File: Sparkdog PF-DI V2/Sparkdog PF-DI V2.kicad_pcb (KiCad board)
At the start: 2 copper layers, 124.5 x 98.9 mm, 3 parts

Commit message: Commit schematic changes, new parts library footprints and step files, PCB design file.
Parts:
- removed IC**: SOP65P1420X360-37N, Samacsys:SOP65P1420X360-37N
- removed REF**: TEENSY_3_5, Sparkdog PF-DI V2:TEENSY_3_5
- removed REF**: ARDUINO_DUE, Sparkdog PF-DI V2:ARDUINO_DUE
- added C200: 0603 1nF, Samacsys:RESC1608X55N, F.Cu at (150.1, 104.0)
- added C201: 0603 1nF, Samacsys:RESC1608X55N, F.Cu at (131.1, 98.0)
- added C202: 0603 1nF, Samacsys:RESC1608X55N, F.Cu at (149.5, 89.7)
- added C203: 0603 1nF, Samacsys:RESC1608X55N, F.Cu at (150.9, 100.5)
- added C400: 0603 100nF, Samacsys:RESC1608X55N, F.Cu at (54.2, 143.8)
- added C401: 0603 100nF, Samacsys:RESC1608X55N, F.Cu at (54.2, 137.8)
- added C402: 0603 1nF, Samacsys:RESC1608X55N, F.Cu at (54.2, 141.0)
- added C403: 0603 1nF, Samacsys:RESC1608X55N, F.Cu at (51.3, 133.6)
- added C404: 0603 1nF, Samacsys:RESC1608X55N, F.Cu at (51.3, 143.8)
- added C405: 0603 1nF, Samacsys:RESC1608X55N, F.Cu at (51.3, 137.8)
- added C500: 0603 10nF, Samacsys:RESC1608X55N, F.Cu at (79.2, 160.1)
- added C501: 0603 10nF, Samacsys:RESC1608X55N, F.Cu at (107.4, 167.9)
- added C502: 0603 10nF, Samacsys:RESC1608X55N, F.Cu at (82.4, 160.1)
- added C503: 0603 100nF, Samacsys:RESC1608X55N, F.Cu at (78.6, 155.1)
- added C504: 0603 100nF, Samacsys:RESC1608X55N, F.Cu at (102.4, 158.9)
- added C505: 0805 10uF, Samacsys:RESC2012X60N, F.Cu at (59.6, 112.6)
- added C506: 0805 10uF, Samacsys:RESC2012X60N, F.Cu at (59.6, 115.8)
- added C600: 0603 10pF, Samacsys:RESC1608X55N, F.Cu at (126.9, 144.3)
- added C601: 0603 10pF, Samacsys:RESC1608X55N, F.Cu at (126.0, 147.6)
- added C700: 0603 100nF, Samacsys:RESC1608X55N, F.Cu at (60.8, 152.8)
- added C701: 0603 10pF, Samacsys:RESC1608X55N, F.Cu at (150.2, 127.0)
- added C702: 0603 10pF, Samacsys:RESC1608X55N, F.Cu at (137.4, 131.6)
- added CD200: 0603 100nF, Samacsys:RESC1608X55N, F.Cu at (146.4, 89.7)
- added CD400: 0603 100nF, Samacsys:RESC1608X55N, F.Cu at (47.0, 139.3)
- added CD401: 0603 100nF, Samacsys:RESC1608X55N, F.Cu at (47.5, 133.0)
- added CD500: CAP4mm 4.7uF, Samacsys:CAPAE1700X1700N, F.Cu at (115.7, 160.8)
- added CD501: 0603 100nF, Samacsys:RESC1608X55N, F.Cu at (87.5, 154.4)
- added CD502: 0603 100nF, Samacsys:RESC1608X55N, F.Cu at (66.5, 112.6)
- added CD600: 0603 100nF, Samacsys:RESC1608X55N, F.Cu at (125.5, 150.4)
- added CD601: 0603 100nF, Samacsys:RESC1608X55N, F.Cu at (127.0, 132.6)
- added CD602: 0603 100nF, Samacsys:RESC1608X55N, F.Cu at (124.6, 148.1)
- added CD603: 0603 100nF, Samacsys:RESC1608X55N, F.Cu at (108.5, 145.3)
- added CD604: 0603 100nF, Samacsys:RESC1608X55N, F.Cu at (131.6, 134.9)
- added CD605: 0603 100nF, Samacsys:RESC1608X55N, F.Cu at (108.0, 136.4)
- added CD606: 0603 100nF, Samacsys:RESC1608X55N, F.Cu at (128.9, 137.4)
- added CD700: 0603 100nF, Samacsys:RESC1608X55N, F.Cu at (141.5, 141.6)
- added CD701: 0603 100nF, Samacsys:RESC1608X55N, F.Cu at (136.0, 147.1)
- added CD702: CAP4mm 4.7uF, Samacsys:CAPAE430X550N, F.Cu at (141.6, 145.2)
- added CD703: 0603 100nF, Samacsys:RESC1608X55N, F.Cu at (135.4, 134.0)
- added CD704: CAP4mm 4.7uF, Samacsys:CAPAE430X550N, F.Cu at (137.8, 150.7)
- added CD705: 0603 100nF, Samacsys:RESC1608X55N, F.Cu at (129.8, 133.3)
- added CD706: 0603 100nF, Samacsys:RESC1608X55N, F.Cu at (139.7, 137.4)
- added CD707: CAP4mm 4.7uF, Samacsys:CAPAE430X550N, F.Cu at (148.6, 143.4)
- added CD708: 0603 100nF, Samacsys:RESC1608X55N, F.Cu at (148.5, 139.8)
- added CD709: CAP17mm, Samacsys:CAPAE1700X1700N, F.Cu at (39.9, 160.9)
- added CD710: 0603 100nF, Samacsys:RESC1608X55N, F.Cu at (137.2, 140.0)
- added CD711: CAP4mm 4.7uF, Samacsys:CAPAE430X550N, F.Cu at (73.9, 168.1)
- added CD712: 0603 100nF, Samacsys:RESC1608X55N, F.Cu at (148.5, 151.4)
- added CD713: 0603 100nF, Samacsys:RESC1608X55N, F.Cu at (143.8, 139.4)
- added CD714: 0603 100nF, Samacsys:RESC1608X55N, F.Cu at (78.1, 163.8)
- added CD900: 0603 100nF, Samacsys:RESC1608X55N, F.Cu at (126.7, 90.8)
- added CD901: 0603 100nF, Samacsys:RESC1608X55N, F.Cu at (116.7, 82.8)
- added CD902: 0603 100nF, Samacsys:RESC1608X55N, F.Cu at (126.7, 82.8)
- added CD903: 0603 100nF, Samacsys:RESC1608X55N, F.Cu at (116.7, 90.8)
- added D200: BZX84C5V1LT1G, Samacsys:SOT96P237X111-3N, F.Cu at (146.3, 105.0)
- added D201: BZX84C5V1LT1G, Samacsys:SOT96P237X111-3N, F.Cu at (131.6, 100.8)
- added D202: BZX84C5V1LT1G, Samacsys:SOT96P237X111-3N, F.Cu at (150.1, 92.7)
- added D203: BZX84C5V1LT1G, Samacsys:SOT96P237X111-3N, F.Cu at (142.1, 103.1)
- added D300: 0805 LED, Samacsys:RESC2012X60N, F.Cu at (140.3, 114.3)
- added D301: 0805 LED, Samacsys:RESC2012X60N, F.Cu at (142.2, 114.3)
- added D500: 0805 1N4148, Samacsys:RESC2012X60N, F.Cu at (80.5, 155.1)
- added D501: 0805 1N4148, Samacsys:RESC2012X60N, F.Cu at (82.4, 155.1)
- added D502: 0805 1N4148, Samacsys:RESC2012X60N, F.Cu at (57.0, 106.9)
- added D503: 0805 1N4148, Samacsys:RESC2012X60N, F.Cu at (57.0, 108.8)
- added D504: 0805 1N4148, Samacsys:RESC2012X60N, F.Cu at (53.2, 112.0)
- added D700: BYG22B, Samacsys:DIOM5127X229N, F.Cu at (56.9, 159.5)
- added D800: DO-214AC SCHOTTKY, Samacsys:DIOM5127X229N, B.Cu at (50.3, 95.2)
- added D801: DO-214AC 81V, Samacsys:DIOM5127X229N, F.Cu at (29.7, 95.2)
- added D802: DO-214AC SCHOTTKY, Samacsys:DIOM5127X229N, F.Cu at (87.6, 85.9)
- added D803: DO-214AC SCHOTTKY, Samacsys:DIOM5127X229N, F.Cu at (108.0, 85.9)
- added D804: DO-214AC 81V, Samacsys:DIOM5127X229N, F.Cu at (45.4, 127.0)
- added D805: DO-214AC SCHOTTKY, Samacsys:DIOM5127X229N, F.Cu at (49.5, 109.2)
- added D850: DO-214AC SCHOTTKY, Samacsys:DIOM5127X229N, B.Cu at (50.3, 86.4)
- added D851: DO-214AC 81V, Samacsys:DIOM5127X229N, F.Cu at (29.7, 86.4)
- added D852: DO-214AC SCHOTTKY, Samacsys:DIOM5127X229N, F.Cu at (77.5, 85.9)
- added D853: DO-214AC SCHOTTKY, Samacsys:DIOM5127X229N, F.Cu at (97.8, 85.9)
- added J1: Conn_01x06_Female, Sparkdog PF-DI V2:SIP-6, F.Cu at (59.3, 83.9)
- added J2: Conn_01x08_Female, Sparkdog PF-DI V2:SIP-8, F.Cu at (47.6, 172.2)
- added J3: Conn_01x06_Female, Sparkdog PF-DI V2:SIP-6, F.Cu at (59.3, 90.3)
- added J4: Conn_01x08_Female, Sparkdog PF-DI V2:SIP-8, F.Cu at (33.7, 111.0)
- added J5: Conn_01x06_Female, Sparkdog PF-DI V2:SIP-6, F.Cu at (59.3, 86.5)
- added J600: M50-3610542R, Samacsys:M503610542, F.Cu at (98.9, 142.4)
- added J700: SSM-106-L-SV, Samacsys:SSM106LSV, F.Cu at (148.1, 115.8)
- added L700: 0805 10nH, Samacsys:RESC2012X60N, F.Cu at (130.0, 129.5)
- added L701: 0805 10nH, Samacsys:RESC2012X60N, F.Cu at (130.0, 131.6)
- added L702: SRN8040-680, Samacsys:INDC8566X410N, F.Cu at (65.4, 167.8)
- added R200: 1206 0.1R, Samacsys:RESC3216X60N, F.Cu at (137.0, 84.3)
- added R201: 1206 0.1R, Samacsys:RESC3216X60N, F.Cu at (140.7, 88.9)
- added R400: 0603 4.7k, Samacsys:RESC1608X55N, F.Cu at (54.2, 139.6)
- added R401: 0603 4.7k, Samacsys:RESC1608X55N, F.Cu at (54.2, 132.2)
- added R402: 0603 47k, Samacsys:RESC1608X55N, F.Cu at (51.3, 139.6)
- added R403: 0603 47k, Samacsys:RESC1608X55N, F.Cu at (51.3, 135.0)
- added R404: 0603 47k, Samacsys:RESC1608X55N, F.Cu at (51.3, 141.0)
- added R405: 0603 47k, Samacsys:RESC1608X55N, F.Cu at (51.3, 132.2)
- added R406: 0603 1k, Samacsys:RESC1608X55N, F.Cu at (51.3, 142.4)
- added R407: 0603 1k, Samacsys:RESC1608X55N, F.Cu at (51.3, 136.4)
- added R408: 0603 1k, Samacsys:RESC1608X55N, F.Cu at (54.2, 142.4)
- added R409: 0603 1k, Samacsys:RESC1608X55N, F.Cu at (54.2, 136.4)
- added R500: 0603 100k, Samacsys:RESC1608X55N, F.Cu at (79.2, 158.8)
- added R501: 0603 100k, Samacsys:RESC1608X55N, F.Cu at (107.4, 166.5)
- added R502: 0603 1k, Samacsys:RESC1608X55N, F.Cu at (79.2, 161.5)
- added R503: 0603 1k, Samacsys:RESC1608X55N, F.Cu at (103.6, 161.0)
- added R504: 2512 0.1R, Samacsys:RESC6331X75N, F.Cu at (81.8, 167.1)
- added R505: 2512 0.1R, Samacsys:RESC6331X75N, F.Cu at (103.6, 167.1)
- added R506: 0603 100R, Samacsys:RESC1608X55N, F.Cu at (82.4, 158.2)
- added R507: 0805 0R, Samacsys:RESC2012X60N, F.Cu at (53.0, 168.7)
- added R508: 0805 0R, Samacsys:RESC2012X60N, F.Cu at (105.5, 155.7)
- added R509: 0805 0R, Samacsys:RESC2012X60N, F.Cu at (104.1, 127.0)
- added R510: 0805 0R, Samacsys:RESC2012X60N, F.Cu at (107.3, 171.7)
- added R511: 0603 10k, Samacsys:RESC1608X55N, F.Cu at (141.2, 168.3)
- added R512: 0603 47k, Samacsys:RESC1608X55N, F.Cu at (56.4, 111.4)
- added R513: 0603 820k, Samacsys:RESC1608X55N, F.Cu at (107.4, 169.7)
- added R514: 0603 5M, Samacsys:RESC1608X55N, F.Cu at (62.7, 117.1)
- added R515: 0603 470k, Samacsys:RESC1608X55N, F.Cu at (65.9, 115.2)
- added R600: 0603 1k, Samacsys:RESC1608X55N, F.Cu at (126.9, 142.1)
- added R700: 0603 1k, Samacsys:RESC1608X55N, F.Cu at (63.9, 152.8)
- added R701: 0603 1k, Samacsys:RESC1608X55N, F.Cu at (56.9, 153.4)
- added R702: 0603 22k, Samacsys:RESC1608X55N, F.Cu at (56.9, 154.9)
- added R703: 0603 22k, Samacsys:RESC1608X55N, F.Cu at (56.9, 156.5)
- added R704: 2512 1R, Samacsys:RESC6331X75N, F.Cu at (31.5, 145.0)
- added R705: 0603 100k, Samacsys:RESC1608X55N, F.Cu at (143.0, 122.4)
- added R706: 0603 1k, Samacsys:RESC1608X55N, F.Cu at (149.9, 134.9)
- added R800: 0603 470R, Samacsys:RESC1608X55N, F.Cu at (46.2, 97.8)
- added R801: 1206 4.7k, Samacsys:RESC3216X60N, F.Cu at (32.5, 95.2)
- added R802: 2512 0.05R, Samacsys:RESC6331X75N, F.Cu at (56.1, 97.8)
- added R803: 0603 10k, Samacsys:RESC1608X55N, F.Cu at (63.4, 94.4)
- added R804: 0603 4.7k, Samacsys:RESC1608X55N, F.Cu at (82.5, 94.0)
- added R805: 0603 10k, Samacsys:RESC1608X55N, F.Cu at (79.5, 94.0)
- added R806: 0603 4.7k, Samacsys:RESC1608X55N, F.Cu at (102.9, 94.0)
- added R807: 0603 1k, Samacsys:RESC1608X55N, F.Cu at (65.7, 99.1)
- added R808: 0603 10k, Samacsys:RESC1608X55N, F.Cu at (99.8, 94.0)
- added R809: 0603 10k, Samacsys:RESC1608X55N, F.Cu at (102.9, 95.5)
- added R810: 2512 0.2R, Samacsys:RESC6331X75N, F.Cu at (52.1, 121.9)
- added R811: 0603 220R, Samacsys:RESC1608X55N, F.Cu at (51.6, 127.0)
- added R812: 0603 10k, Samacsys:RESC1608X55N, F.Cu at (50.8, 115.6)
- added R850: 0603 470R, Samacsys:RESC1608X55N, F.Cu at (46.2, 88.9)
- added R851: 1206 4.7k, Samacsys:RESC3216X60N, F.Cu at (32.5, 86.2)
- added R852: 2512 0.05R, Samacsys:RESC6331X75N, F.Cu at (56.1, 94.0)
- added R853: 0603 10k, Samacsys:RESC1608X55N, F.Cu at (72.4, 95.5)
- added R854: 0603 4.7k, Samacsys:RESC1608X55N, F.Cu at (72.4, 94.0)
- added R855: 0603 10k, Samacsys:RESC1608X55N, F.Cu at (68.6, 95.2)
- added R856: 0603 4.7k, Samacsys:RESC1608X55N, F.Cu at (92.7, 94.0)
- added R857: 0603 1k, Samacsys:RESC1608X55N, F.Cu at (62.7, 99.1)
- added R858: 0603 10k, Samacsys:RESC1608X55N, F.Cu at (68.6, 94.0)
- added R859: 0603 10k, Samacsys:RESC1608X55N, F.Cu at (89.8, 94.0)
- added RN100: 1206 10k, Samacsys:742C083103JP, F.Cu at (111.1, 128.3)
- added RN101: 1206 1k, Samacsys:742C083103JP, F.Cu at (106.7, 130.8)
- added RN102: 1206 1k, Samacsys:742C083103JP, F.Cu at (128.3, 135.9)
- added RN103: 1206 1k, Samacsys:742C083103JP, F.Cu at (78.5, 115.1)
- added RN104: 1206 10k, Samacsys:742C083103JP, F.Cu at (137.2, 117.9)
- added RN105: 1206 1k, Samacsys:742C083103JP, F.Cu at (149.4, 96.6)
- added RN200: 1206 10k, Samacsys:742C083103JP, F.Cu at (140.7, 85.1)
- added RN201: 1206 10k, Samacsys:742C083103JP, F.Cu at (135.6, 95.9)
- added RN202: 1206 10k, Samacsys:742C083103JP, F.Cu at (135.6, 101.0)
- added RN203: 1206 470R, Samacsys:742C083103JP, F.Cu at (142.0, 93.3)
- added RN204: 1206 10k, Samacsys:742C083103JP, F.Cu at (141.9, 106.9)
- added RN205: 1206 10k, Samacsys:742C083103JP, F.Cu at (148.1, 100.8)
- added RN300: 1206 1k, Samacsys:742C083103JP, F.Cu at (137.2, 114.3)
- added RN400: 220k, Samacsys:742C083103JP, F.Cu at (46.8, 130.8)
- added RN401: 220R, Samacsys:742C083103JP, F.Cu at (43.2, 135.3)
- added RN402: 220k, Samacsys:742C083103JP, F.Cu at (43.2, 142.0)
- added RN500: 1206 180k, Samacsys:742C083103JP, F.Cu at (56.1, 115.1)
- added RN501: 1206 10k, Samacsys:742C083103JP, F.Cu at (60.8, 108.8)
- added RN600: 1206 10k, Samacsys:742C083103JP, F.Cu at (106.7, 134.1)
- added RN601: 1206 100k, Samacsys:742C083103JP, F.Cu at (106.7, 142.2)
- added RN602: 1206 10k, Samacsys:742C083103JP, F.Cu at (114.9, 128.3)
- added RN603: 1206 10k, Samacsys:742C083103JP, F.Cu at (122.6, 128.3)
- added RN604: 1206 1k, Samacsys:742C083103JP, F.Cu at (120.7, 149.2)
- added RN605: 1206 10k, Samacsys:742C083103JP, F.Cu at (118.7, 128.3)
- added RN606: 1206 10k, Samacsys:742C083103JP, F.Cu at (106.7, 138.8)
- added U2: Arduino_Footprint, Sparkdog PF-DI V2:ARDUINO_DUE, F.Cu at (132.7, 152.9)
- added U200: IRF7907TRPBF, Samacsys:SOIC127P600X175-8N, F.Cu at (147.7, 85.1)
- added U201: Dual_Trans_Array_NPN, Sparkdog PF-DI V2:SOT-363-6, F.Cu at (135.6, 88.9)
- added U202: Dual_Trans_Array_NPN, Sparkdog PF-DI V2:SOT-363-6, F.Cu at (135.6, 91.4)
- added U203: Dual_Trans_Array_PNP, Sparkdog PF-DI V2:SOT-363-6, F.Cu at (133.7, 90.2)
- added U204: Dual_Trans_Array_PNP, Sparkdog PF-DI V2:SOT-363-6, F.Cu at (133.7, 92.7)
- added U205: 74AHC14PW,118, Samacsys:SOP65P640X110-14N, F.Cu at (142.0, 98.4)
- added U300: Teensy_3_5, Sparkdog PF-DI V2:TEENSY_3_5, F.Cu at (134.6, 123.2)
- added U400: TLV9052, Samacsys:SOT65P280X110-8N, F.Cu at (47.4, 142.0)
- added U401: TLV9052, Samacsys:SOT65P280X110-8N, F.Cu at (47.4, 135.1)
- added U500: L6206PD013TR, Samacsys:SOP65P1420X360-37N, F.Cu at (92.8, 162.1)
- added U501: SUD19P06-60, Sparkdog PF-DI V2:MDAC-TO-252-3, F.Cu at (131.7, 168.3)
- added U502: TL331SN4T3G, Samacsys:SOT95P275X110-5N, F.Cu at (62.7, 113.9)
- added U503: Dual_Trans_Array_NPN, Sparkdog PF-DI V2:SOT-363-6, F.Cu at (64.0, 109.5)
- added U600: MK10DX128VLK7, Sparkdog PF-DI V2:MK10DX128VLK7, F.Cu at (117.5, 139.1)
- added U601: TLV809EA29DCKR, Samacsys:SOT65P210X110-3N, F.Cu at (126.9, 139.6)
- added U700: BD433M5FP-CE2, Sparkdog PF-DI V2:MDAC-TO-252-3, F.Cu at (139.8, 161.0)
- added U701: PIC18F26J50T-I_ML, Sparkdog PF-DI V2:PIC18F26, F.Cu at (144.8, 134.6)
- added U702: TCAN334, Samacsys:SOIC127P600X175-8N, F.Cu at (64.8, 134.9)
- added U703: BD433M5FP-CE2, Sparkdog PF-DI V2:MDAC-TO-252-3, F.Cu at (148.5, 161.0)
- added U704: LM2577SX-ADJ_NOPB, Samacsys:KTT0005B, F.Cu at (74.5, 158.8)
- added U800: DDC113TU, Sparkdog PF-DI V2:SOT-363-6, F.Cu at (76.2, 96.5)
- added U801: DDC113TU, Sparkdog PF-DI V2:SOT-363-6, F.Cu at (106.7, 96.3)
- added U802: DDC113TU, Sparkdog PF-DI V2:SOT-363-6, F.Cu at (45.2, 94.7)
- added U803: STD7NK40Z, Sparkdog PF-DI V2:MDAC-TO-252-3, F.Cu at (36.8, 95.2)
- added U804: STD7NK40Z, Sparkdog PF-DI V2:MDAC-TO-252-3, B.Cu at (45.7, 95.2)
- added U805: SUD19P06-60, Sparkdog PF-DI V2:MDAC-TO-252-3, F.Cu at (82.5, 85.1)
- added U806: SUD19P06-60, Sparkdog PF-DI V2:MDAC-TO-252-3, B.Cu at (82.5, 97.8)
- added U807: SUD19P06-60, Sparkdog PF-DI V2:MDAC-TO-252-3, B.Cu at (102.9, 97.8)
- added U808: SUD19P06-60, Sparkdog PF-DI V2:MDAC-TO-252-3, F.Cu at (102.9, 85.1)
- added U809: Dual_Trans_Array_NPN, Sparkdog PF-DI V2:SOT-363-6, F.Cu at (55.4, 121.2)
- added U810: STD7NK40Z, Sparkdog PF-DI V2:MDAC-TO-252-3, F.Cu at (45.5, 117.6)
- added U811: STD7NK40Z, Sparkdog PF-DI V2:MDAC-TO-252-3, B.Cu at (45.7, 109.2)
- added U850: DDC113TU, Sparkdog PF-DI V2:SOT-363-6, F.Cu at (96.5, 96.5)
- added U851: DDC113TU, Sparkdog PF-DI V2:SOT-363-6, F.Cu at (86.4, 96.5)
- added U852: DDC113TU, Sparkdog PF-DI V2:SOT-363-6, F.Cu at (31.8, 90.2)
- added U853: STD7NK40Z, Sparkdog PF-DI V2:MDAC-TO-252-3, F.Cu at (36.8, 86.4)
- added U854: STD7NK40Z, Sparkdog PF-DI V2:MDAC-TO-252-3, B.Cu at (45.7, 86.4)
- added U855: SUD19P06-60, Sparkdog PF-DI V2:MDAC-TO-252-3, F.Cu at (72.4, 86.4)
- added U856: SUD19P06-60, Sparkdog PF-DI V2:MDAC-TO-252-3, B.Cu at (72.4, 97.8)
- added U857: SUD19P06-60, Sparkdog PF-DI V2:MDAC-TO-252-3, B.Cu at (92.7, 97.8)
- added U858: SUD19P06-60, Sparkdog PF-DI V2:MDAC-TO-252-3, F.Cu at (92.7, 85.1)
- added U900: SN74AHCT02, Samacsys:SOP65P640X110-14N, F.Cu at (126.0, 86.4)
- added U901: SN74AHCT02, Samacsys:SOP65P640X110-14N, F.Cu at (116.0, 86.4)
- added U902: SN74AHCT08, Samacsys:SOP65P640X110-14N, F.Cu at (126.0, 94.4)
- added U903: SN74AHCT08, Samacsys:SOP65P640X110-14N, F.Cu at (116.0, 94.4)
- added X600: Crystal, Samacsys:ECS49205PXTR, F.Cu at (131.4, 146.2)
- added X700: 4 MHz, Samacsys:ECS49205PXTR, F.Cu at (141.2, 127.8)
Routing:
- net VSS: track 0.00 -> 320.5 mm, vias 0 -> 1
- net /VVT_INP4: track 0.00 -> 96.5 mm
- net /VVT_INP3: track 0.00 -> 90.2 mm
- net /VVT_INP1: track 0.00 -> 84.1 mm
- net /VVT_INP2: track 0.00 -> 81.9 mm
- net VCC50VPP: track 0.00 -> 69.4 mm
- net /CAN_RX: track 0.00 -> 58.3 mm
- net /CAN_TX: track 0.00 -> 58.3 mm
- net /GDI1_SIG_s: track 0.00 -> 54.9 mm, vias 0 -> 2
- net /PWIOB+: track 0.00 -> 51.6 mm, vias 0 -> 1
- net /GDI2_SIG_s: track 0.00 -> 50.5 mm, vias 0 -> 1
- net VCC12VP: track 0.00 -> 50.4 mm
- net /PWIOCD-: track 0.00 -> 47.4 mm
- net /TPSS: track 0.00 -> 40.1 mm, vias 0 -> 1
- net /PWIOD+: track 0.00 -> 39.9 mm, vias 0 -> 1
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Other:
- copper layers 2 -> 4
- net class GDI_LS_Width added: clearance 0.254, trace_width 0.762, via_dia 0.8, via_drill 0.4
- net class VCC50V added: clearance 0.254, trace_width 1.524, via_dia 0.8, via_drill 0.4
- net class VSS added: clearance 0.2, trace_width 0.5, via_dia 0.8, via_drill 0.4

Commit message: Commit running changes for safekeeping
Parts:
- moved R508 55.3 mm to (51.4, 167.3), turned to 0 degrees
- moved R509 25.3 mm to (85.9, 144.5)
- moved R510 17.5 mm to (104.5, 154.4)
- moved U802 14.1 mm to (31.8, 99.1)
- moved J4 5.08 mm to (33.7, 116.1)
- moved CD710 3.69 mm to (140.8, 139.8), turned to 0 degrees
- moved R705 2.33 mm to (141.4, 124.1), turned to 180 degrees
- moved CD703 2.13 mm to (137.4, 133.3)
- moved R507 1.65 mm to (51.4, 169.3)
- moved CD500 1.52 mm to (117.2, 160.8)
- moved CD501 1.52 mm to (87.5, 152.9)
- moved L700 1.28 mm to (128.8, 129.7)
- moved R812 0.80 mm to (50.5, 116.3)
- moved L701 0.51 mm to (129.5, 131.6)
- moved R706 0.28 mm to (150.1, 134.7)
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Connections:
- J4 pad 1: VSS -> Net-(J4-Pad1)
- J4 pad 2: VSS -> Net-(J4-Pad2)
- J4 pad 3: VSS -> Net-(J4-Pad3)
- J4 pad 4: VSS -> Net-(J4-Pad4)
- J4 pad 5: VSS -> Net-(J4-Pad5)
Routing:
- net VSS: track 320.5 -> 494.2 mm, vias 1 -> 8
- net /MOSI: track 0.00 -> 160.6 mm, vias 0 -> 4
- net /SCLK: track 0.00 -> 158.6 mm, vias 0 -> 4
- net /5 ETC/ETC_PEN: track 3.84 -> 162.3 mm, vias 0 -> 2
- net VBATT: track 3.97 -> 149.8 mm, vias 0 -> 1
- net /7 POWER/SIG_KAL: track 0.00 -> 139.1 mm, vias 0 -> 2
- net /VSDC: track 0.00 -> 129.1 mm, vias 0 -> 1
- net /9 GDI CONTROL/SIGAB_LS_EN: track 0.00 -> 117.1 mm, vias 0 -> 2
- net /MISO: track 0.00 -> 115.1 mm, vias 0 -> 3
- net /PUBEN: track 0.00 -> 113.1 mm, vias 0 -> 1
- net /IEN: track 0.00 -> 113.0 mm, vias 0 -> 1
- net /8 GDI/SIG_PUMP_PWMS: track 0.00 -> 110.5 mm, vias 0 -> 2
- net /RPS: track 0.00 -> 110.3 mm, vias 0 -> 1
- net /HS1EN: track 0.00 -> 107.9 mm
- net /9 GDI CONTROL/SIGCD_LS_EN: track 0.00 -> 107.8 mm, vias 0 -> 2
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- added copper zone on In2.Cu, net VSS

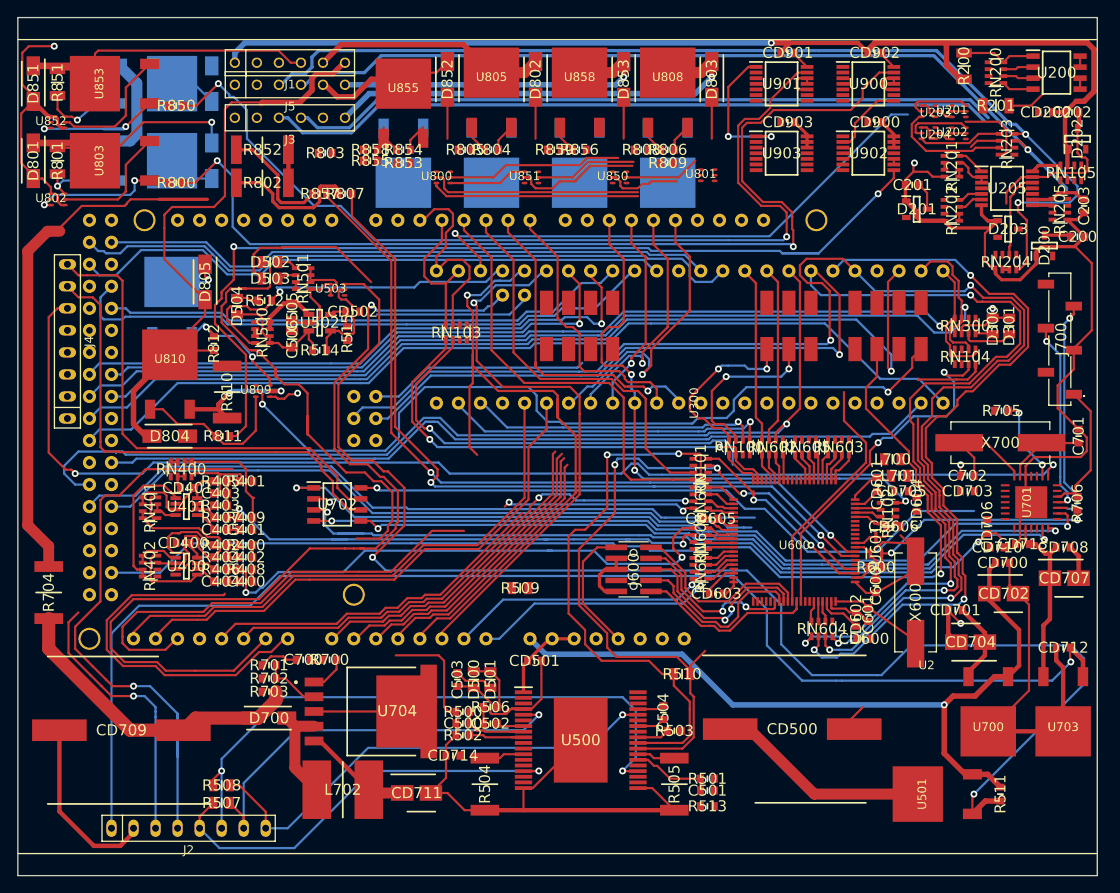
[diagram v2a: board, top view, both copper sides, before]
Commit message: Commit updates and Teensy schematic footprint correction.
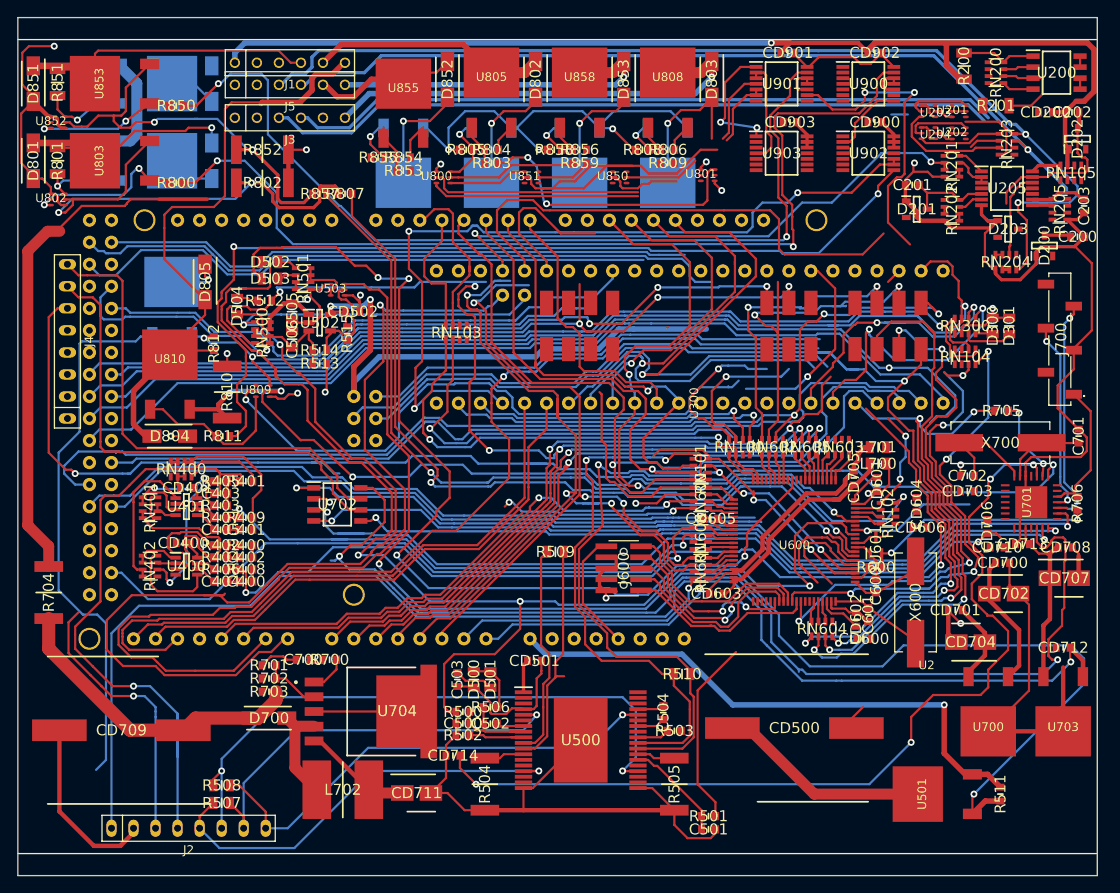
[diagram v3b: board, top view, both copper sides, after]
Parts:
- moved R513 67.9 mm to (62.7, 118.6)
- moved R858 21.2 mm to (89.8, 94.0), turned to 0 degrees
- moved R803 19.2 mm to (82.5, 95.5), turned to 0 degrees
- moved R509 5.84 mm to (89.9, 140.3)
- moved CD705 5.67 mm to (124.3, 131.8), turned to 90 degrees
- moved C501 4.47 mm to (107.6, 172.3)
- moved R501 4.32 mm to (107.6, 170.8)
- moved L701 4.09 mm to (127.1, 128.3)
- moved R859 3.29 mm to (92.7, 95.5), turned to 0 degrees
- moved CD606 3.05 mm to (132.0, 137.5)
- moved L700 1.73 mm to (127.1, 130.2)
- moved J600 1.15 mm to (97.8, 142.2)
- moved R855 0.97 mm to (69.5, 94.9), turned to 0 degrees
- moved R853 0.89 mm to (72.4, 96.4)
- moved R854 0.89 mm to (72.4, 94.9)
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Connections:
- CD603 pad 2: VCC3V3A -> VCCA3V3
- U300 pad 25: /SWH -> /TPSS
- U300 pad 26: /SWL -> /2 VVT/PULLEN_AB
- U300 pad 27: /IEN -> /CMPS_SIG
- U300 pad 28: Net-(U300-Pad28) -> /CKPS_SIG
- U300 pad 29: /MOSI -> /3 TEENSY/GDI2_SIG
- U300 pad 30: /MISO -> /3 TEENSY/GDI1_SIG
- U300 pad 31: /SCLK -> /PPSM
- U300 pad 32: /PUBEN -> /DAC_UEGO
- U300 pad 33: /VRAEN -> /VSDC
- U300 pad 34: /VRBEN -> VSS
- U300 pad 35: /M1EN -> /SIG_PUMP_EN
- U300 pad 36: /REL_CS -> /SIG_VVTA_OUT
- U300 pad 37: Net-(U300-Pad37) -> /CTS
- U300 pad 38: /M2EN -> /PPSS
- U300 pad 39: /HMEN -> /TPSM
- U300 pad 40: /PUAEN -> /RPS
- U300 pad 41: /HYSTLAB -> /BATT
- U300 pad 42: /HYSTHAB -> /SIG_VVT4_IN
- U300 pad 43: /ACH -> /SIG_VVT3_IN
- U300 pad 44: /ACL -> /SIG_VVT2_IN
- U300 pad 45: /TPSS -> /SIG_VVT1_IN
- U300 pad 46: /2 VVT/PULLEN_AB -> VCC3V3
- U300 pad 47: /CMPS_SIG -> VSS
- U300 pad 48: /CKPS_SIG -> VCC5V
- U300 pad 49: /3 TEENSY/GDI2_SIG -> /SWH
- U300 pad 50: /3 TEENSY/GDI1_SIG -> /SWL
- U300 pad 51: /PPSM -> /IEN
- U300 pad 52: /DAC_UEGO -> Net-(U300-Pad52)
- U300 pad 53: /VSDC -> /MOSI
- U300 pad 54: VSS -> /MISO
- U300 pad 55: /SIG_PUMP_EN -> /SCLK
- U300 pad 56: /SIG_VVTA_OUT -> /PUBEN
- U300 pad 57: /CTS -> /VRAEN
- U300 pad 58: /PPSS -> /VRBEN
- U300 pad 59: /TPSM -> /M1EN
- U300 pad 60: /RPS -> /REL_CS
- U300 pad 61: /BATT -> /M2EN
- U300 pad 62: /SIG_VVT4_IN -> /3 TEENSY/REL_RST
- U300 pad 63: /SIG_VVT3_IN -> /HMEN
- U300 pad 64: /SIG_VVT2_IN -> /PUAEN
- U300 pad 65: /SIG_VVT1_IN -> /HYSTLAB
- U300 pad 66: VCC3V3 -> /HYSTHAB
- U300 pad 67: VSS -> /ACH
- U300 pad 68: VCC5V -> /ACL
- U600 pad 17: VCC3V3A -> VCCA3V3
- U600 pad 18: VCC3V3A -> VCCA3V3
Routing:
- net /5 ETC/ETC_ENB: track 18.8 -> 137.7 mm, vias 0 -> 4
- net Net-(CD714-Pad1): track 0.00 -> 105.8 mm, vias 0 -> 4
- net /TPSM: track 60.4 -> 158.6 mm, vias 0 -> 2
- net /SIG_GDIP_EN: track 0.65 -> 95.0 mm, vias 0 -> 3
- net /SIG_PUMP_IF: track 14.5 -> 93.0 mm, vias 2 -> 4
- net /5 ETC/ETC_ENA: track 69.5 -> 147.1 mm, vias 0 -> 3
- net VCC5V: track 23.8 -> 96.3 mm, vias 0 -> 2
- net /SIG_VVT1_IN: track 0.80 -> 66.4 mm, vias 0 -> 2
- net /2 VVT/PULLEN_AB: track 66.9 -> 3.20 mm, vias 1 -> 0
- net /SIGCD_PWM: track 0.00 -> 60.8 mm, vias 0 -> 5
- net /TPSS: track 75.7 -> 136.3 mm, vias 1 -> 5
- net /SIG_VVT2_IN: track 0.00 -> 60.4 mm
- net /DAC_UEGO: track 53.0 -> 113.2 mm, vias 0 -> 1
- net Net-(U701-Pad19): track 75.7 -> 130.7 mm, vias 1 -> 2
- net VCC12VP: track 102.8 -> 155.2 mm
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
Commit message: Commit for safekeeping
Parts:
- moved CD604 10.3 mm to (126.5, 125.9), turned to 270 degrees
- moved CD606 0.85 mm to (132.3, 136.8), turned to 270 degrees
- moved RN100 0.64 mm to (110.6, 127.9)
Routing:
- net VCC3V3: track 48.2 -> 400.2 mm, vias 0 -> 12
- net VCC5V: track 96.3 -> 293.5 mm, vias 2 -> 14
- net /SIGAB_LVEN: track 24.5 -> 167.0 mm, vias 0 -> 3
- net /6 ETC PROCESSOR/A12: track 0.00 -> 114.6 mm, vias 0 -> 4
- net /SIGCD_LVEN: track 16.4 -> 112.0 mm, vias 0 -> 4
- net /TPSS: track 136.3 -> 226.8 mm
- net /SIGCD_PEAK: track 3.02 -> 87.6 mm, vias 0 -> 5
- net /SIGAB_PWM: track 3.14 -> 87.1 mm, vias 0 -> 2
- net /INJ3_SIG: track 34.7 -> 115.9 mm, vias 1 -> 4
- net /SIG_VVTA_OUT: track 0.00 -> 76.9 mm, vias 0 -> 1
- net VCC12VP: track 155.2 -> 231.2 mm, vias 1 -> 5
- net /M1EN: track 76.4 -> 151.7 mm, vias 0 -> 3
- net /CMPS_SIG: track 16.7 -> 91.1 mm, vias 0 -> 4
- net VCC12V: track 62.3 -> 136.0 mm, vias 3 -> 6
- net /SIG_VVTB_OUT: track 0.00 -> 73.5 mm, vias 0 -> 2
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
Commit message: Commit all files up to 21072021 Gerber and drill outputs.
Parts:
- added C100: 0603 100nF, Samacsys:RESC1608X55N, F.Cu at (52.8, 153.9)
- added R100: 0603 1k, Samacsys:RESC1608X55N, F.Cu at (41.2, 107.8)
- added R101: 0603 1k, Samacsys:RESC1608X55N, F.Cu at (91.3, 137.5)
- added R601: 0603 1k, Samacsys:RESC1608X55N, F.Cu at (139.7, 137.2)
- added RN106: 1206 10k, Samacsys:742C083103JP, F.Cu at (52.6, 157.6)
- moved CD706 79.7 mm to (60.1, 134.9)
- moved CD710 74.2 mm to (73.9, 171.8)
- moved CD605 4.44 mm to (103.4, 136.5)
- moved D700 3.54 mm to (56.0, 162.9)
- moved RN100 1.40 mm to (110.6, 126.5)
- moved R509 1.08 mm to (88.8, 140.3)
- moved RN101 0.77 mm to (106.8, 130.0)
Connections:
- CD710 pad 1: VCC12VP -> VCC12VPP
- CD711 pad 1: VCC12VP -> VCC12VPP
- J1 pad 2: VCC12 -> VCC12VPP
- L702 pad 1: VCC12VP -> VCC12VPP
- R400 pad 2: /SIG_K2IN -> /SIG_K1IN
- R511 pad 1: VCC12VP -> VCC12VPP
- R512 pad 1: /TPSS -> /TPSM
- R600 pad 2: Net-(R600-Pad2) -> /6 ETC PROCESSOR/RESET
- R805 pad 1: VCC12V -> VCC12VPP
- R808 pad 1: VCC12V -> VCC12VPP
- R855 pad 1: VCC12V -> VCC12VPP
- R858 pad 1: VCC12V -> VCC12VPP
- RN500 pad 1: /TPSM -> /PPSM
- RN500 pad 4: /TPSS -> /TPSM
- U2 pad 25: Net-(U2-Pad25) -> VSS
- U2 pad 26: Net-(U2-Pad26) -> VSS
- U2 pad 59: Net-(U2-Pad59) -> VCC5V
- U2 pad 60: Net-(U2-Pad60) -> VCC5V
- U501 pad 3: VCC12VP -> VCC12VPP
- U600 pad 31: /6 ETC PROCESSOR/RESET -> Net-(U600-Pad31)
- U600 pad 42: Net-(R600-Pad2) -> /6 ETC PROCESSOR/RESET
- U701 pad 10: Net-(U701-Pad10) -> /SIG_K1O
- U701 pad 14: Net-(U701-Pad14) -> /SIG_KTX
- U701 pad 28: Net-(U701-Pad28) -> /SIG_K2O
- U704 pad 5: VCC12VP -> VCC12VPP
- U802 pad 2: /8 GDI/SIG_LSAB_OFF -> /GDI1_SIG_s
- U804 pad 3: VCC12V -> VCC12VPP
- U806 pad 3: VCC12V -> VCC12VPP
- U807 pad 3: VCC12V -> VCC12VPP
- U811 pad 3: VCC12VP -> VCC12VPP
- U852 pad 2: /8 GDI/SIG_LDCD_OFF -> /GDI2_SIG_s
- U854 pad 3: VCC12V -> VCC12VPP
- U856 pad 3: VCC12V -> VCC12VPP
- U857 pad 3: VCC12V -> VCC12VPP
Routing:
- net VCC12VPP: track 0.00 -> 420.0 mm, vias 0 -> 9
- net VCC12VP: track 231.2 -> 78.0 mm, vias 5 -> 1
- net /SIG_K1O: track 66.7 -> 215.0 mm, vias 2 -> 3
- net /SIG_K2O: track 63.1 -> 206.2 mm, vias 2 -> 3
- net VCC12V: track 136.0 -> 0.00 mm, vias 6 -> 0
- net /SIG_VVTB_OUT: track 73.5 -> 162.3 mm, vias 2 -> 4
- net /TPSS: track 226.8 -> 143.7 mm, vias 5 -> 2
- net VCC3V3K: track 158.7 -> 237.8 mm, vias 3 -> 2
- net /PPSM: track 116.5 -> 185.1 mm, vias 4 -> 5
- net /TPSM: track 192.3 -> 259.5 mm, vias 5 -> 7
- net /GDI2_SIG_s: track 55.2 -> 122.3 mm, vias 2 -> 4
- net /GDI1_SIG_s: track 56.0 -> 122.6 mm, vias 2 -> 4
- net VCC3V3: track 400.2 -> 465.9 mm, vias 12 -> 13
- net /HMEN: track 67.8 -> 124.3 mm, vias 1 -> 2
- net /7 POWER/SIG_KAL: track 149.4 -> 192.2 mm, vias 2 -> 5
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- added copper zone on B.Cu, net VSS
- added copper zone on F.Cu, net VSS
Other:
- board text added: "Sparkdog PF-DI V2 (c) MDAC 2021"
